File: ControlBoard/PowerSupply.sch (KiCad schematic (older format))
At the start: 6 parts, among them CON1 BARREL_JACK, J1 OrangePiPrime, M1 DC-DC_REG

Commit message: Revision 1.2 of the Control Board - All resisitors to 10k - Add solder jumpers to set i2c address - Move the GPIO +V line to 3.3V - Move pushbutton to PA6 as it has an interrupt associated with it - Update copyright year - Add OSHW & Inferno Embedded logos that was lost - Use SMD 28V zener for ESD protection on the 28V line - Use SMD 5.1V zener for ESD protection on the 5V line - Add a 2A polyswitch (fuse) to protect against overcurrent through the PSU - Switch the dc-dc footprint to SMD pads - Switch from electrolytic to ceramic caps (cheaper, easier to install) - Add a cutout for access to the serial header
Signed-off-by: Alastair D'Silva <alastair@d-silva.org>
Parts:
- added F1: Polyfuse, Fuse:Fuse_1206_3216Metric, symbol Device:Polyfuse
- C2: value 100uF -> 100uF 50V; footprint Capacitors_SMD:CP_Elec_6.3x7.7 -> Capacitor_SMD:C_1206_3216Metric
- C3, C4: value 100uF -> 100uF 16V; footprint Capacitors_SMD:CP_Elec_6.3x7.7 -> Capacitor_SMD:C_1206_3216Metric
- CON1: symbol conn:BARREL_JACK -> ControlBoard-rescue:BARREL_JACK-conn
- J1: symbol OrangePi:OrangePiPrime -> ControlBoard-rescue:OrangePiPrime-OrangePi
- M1: footprint D-Sun DC-DC Regulator:D-SUN_DC_DC -> DC-DC:D-SUN_DC_DC; symbol dc-dc_regulator:DC-DC_REG -> ControlBoard-rescue:DC-DC_REG-dc-dc_regulator
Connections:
- net +5V: now also F1.1; no longer M1.3 (OUT+)
- new net: F1.2, M1.3 (OUT+)
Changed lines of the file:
@@
 $EndDescr
 $Comp
-L conn:BARREL_JACK CON1
+L ControlBoard-rescue:BARREL_JACK-conn CON1
 U 1 1 5941132E
 P 1700 1150
@@
 	2100 1050 2100 950
 $Comp
-L OrangePi:OrangePiPrime J1
+L ControlBoard-rescue:OrangePiPrime-OrangePi J1
 U 1 1 5946954A
 P 1000 3400
+AR Path="/5946954A" Ref="J1"  Part="1"
+AR Path="/594691E7/5946954A" Ref="J1"  Part="1"
 F 0 "J1" H 1900 4500 60  0000 C CNN
 F 1 "OrangePiPrime" H 1350 4500 60  0000 C CNN
@@
 P 2400 1100
 F 0 "C2" H 2518 1146 50  0000 L CNN
-F 1 "100uF" H 2518 1055 50  0000 L CNN
-F 2 "Capacitors_SMD:CP_Elec_6.3x7.7" H 2438 950 50  0001 C CNN
+F 1 "100uF 50V" H 2518 1055 50  0000 L CNN
+F 2 "Capacitor_SMD:C_1206_3216Metric" H 2438 950 50  0001 C CNN
 F 3 "~" H 2400 1100 50  0001 C CNN
 	1    2400 1100
@@
 P 2550 3150
 F 0 "C3" H 2668 3196 50  0000 L CNN
-F 1 "100uF" H 2668 3105 50  0000 L CNN
-F 2 "Capacitors_SMD:CP_Elec_6.3x7.7" H 2588 3000 50  0001 C CNN
+F 1 "100uF 16V" H 2668 3105 50  0000 L CNN
+F 2 "Capacitor_SMD:C_1206_3216Metric" H 2588 3000 50  0001 C CNN
 F 3 "~" H 2550 3150 50  0001 C CNN
 	1    2550 3150
@@
 Connection ~ 1850 4250
 $Comp
-L dc-dc_regulator:DC-DC_REG M1
+L ControlBoard-rescue:DC-DC_REG-dc-dc_regulator M1
 U 1 1 5BE5E7C7
 P 4650 1450
 F 0 "M1" H 4650 2037 60  0000 C CNN
 F 1 "DC-DC_REG" H 4650 1931 60  0000 C CNN
-F 2 "D-Sun DC-DC Regulator:D-SUN_DC_DC" H 4650 1450 60  0001 C CNN
+F 2 "DC-DC:D-SUN_DC_DC" H 4650 1450 60  0001 C CNN
 F 3 "" H 4650 1450 60  0000 C CNN
 	1    4650 1450
@@
 P 3050 2650
 F 0 "C4" H 3168 2696 50  0000 L CNN
-F 1 "100uF" H 3168 2605 50  0000 L CNN
-F 2 "Capacitors_SMD:CP_Elec_6.3x7.7" H 3088 2500 50  0001 C CNN
+F 1 "100uF 16V" H 3168 2605 50  0000 L CNN
+F 2 "Capacitor_SMD:C_1206_3216Metric" H 3088 2500 50  0001 C CNN
 F 3 "~" H 3050 2650 50  0001 C CNN
 	1    3050 2650
@@
 L power:+5V #PWR0107
 U 1 1 5BE6087B
-P 5650 1100
-F 0 "#PWR0107" H 5650 950 50  0001 C CNN
-F 1 "+5V" H 5650 1240 50  0000 C CNN
-F 2 "" H 5650 1100 50  0000 C CNN
-F 3 "" H 5650 1100 50  0000 C CNN
-	1    5650 1100
-	1    0    0    -1
-$EndComp
-Wire Wire Line
-	5550 1250 5650 1250
-Wire Wire Line
-	5650 1250 5650 1100
+P 6200 1150
+F 0 "#PWR0107" H 6200 1000 50  0001 C CNN
+F 1 "+5V" H 6200 1290 50  0000 C CNN
+F 2 "" H 6200 1150 50  0000 C CNN
+F 3 "" H 6200 1150 50  0000 C CNN
+	1    6200 1150
+	1    0    0    -1
+$EndComp
+$Comp
+L Device:Polyfuse F1
+U 1 1 5C4B0AB6
+P 5900 1250
+F 0 "F1" V 5675 1250 50  0000 C CNN
+F 1 "Polyfuse" V 5766 1250 50  0000 C CNN
+F 2 "Fuse:Fuse_1206_3216Metric" H 5950 1050 50  0001 L CNN
+F 3 "~" H 5900 1250 50  0001 C CNN
+	1    5900 1250
+	0    1    1    0
+$EndComp
+Wire Wire Line
+	5550 1250 5750 1250
+Wire Wire Line
+	6050 1250 6200 1250
+Wire Wire Line
+	6200 1250 6200 1150
 $EndSCHEMATC

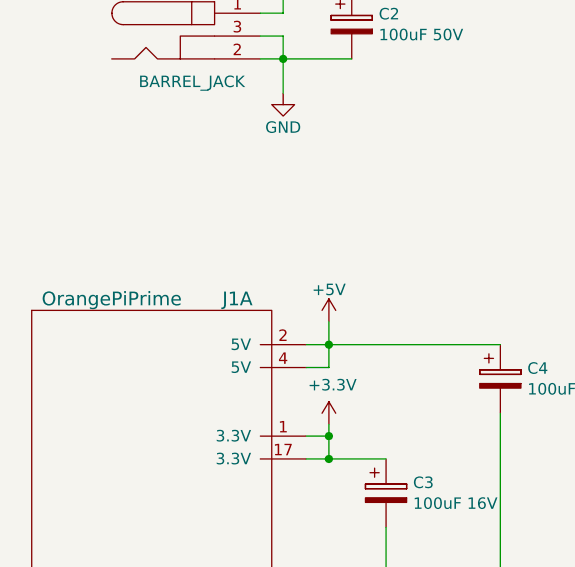
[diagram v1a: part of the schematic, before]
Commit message: Controlboard updates - Add second I2C port - Add Power LEDs (5V & 3.3V) - Add GPIO LED on PA2 - Add header for ST7735 LCD - Add missing mounting holes - Save OrangePiPrime footprints and symbols as explicit libs
Signed-off-by: Alastair D'Silva <alastair@d-silva.org>
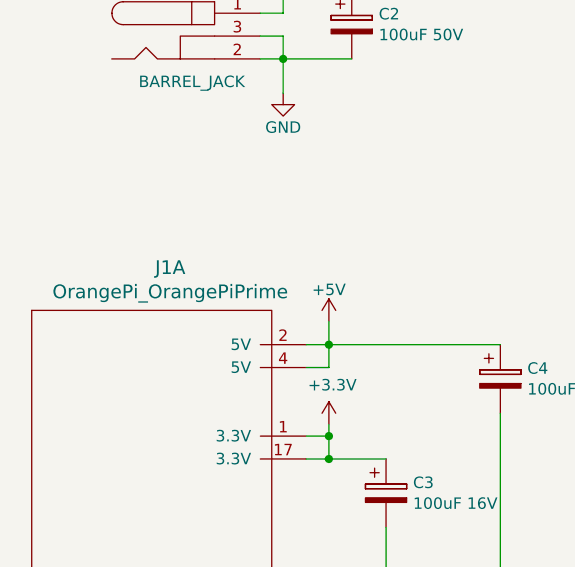
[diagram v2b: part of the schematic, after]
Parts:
- removed J1: OrangePiPrime, OrangePi:OrangePiPrime, symbol ControlBoard-rescue:OrangePiPrime-OrangePi
- added J1: OrangePi_OrangePiPrime, OrangePiPrime:OrangePiPrime, symbol OrangePiPrime:OrangePi_OrangePiPrime
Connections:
- net +3V3: now also J1.1 (3.3V), J1.17 (3.3V)
- net +5V: now also J1.2 (5V), J1.4 (5V)
- net GND: now also J1.14 (Gnd), J1.20 (Gnd), J1.25 (Gnd), J1.30 (Gnd), J1.34 (Gnd), J1.39 (Gnd), J1.6 (Gnd), J1.9 (Gnd)
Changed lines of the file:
@@
 	2100 1050 2100 950
-$Comp
-L ControlBoard-rescue:OrangePiPrime-OrangePi J1
-U 1 1 5946954A
-P 1000 3400
-AR Path="/5946954A" Ref="J1"  Part="1"
-AR Path="/594691E7/5946954A" Ref="J1"  Part="1"
-F 0 "J1" H 1900 4500 60  0000 C CNN
-F 1 "OrangePiPrime" H 1350 4500 60  0000 C CNN
-F 2 "OrangePi:OrangePiPrime" H 1000 3400 60  0001 C CNN
-F 3 "" H 1000 3400 60  0000 C CNN
-	1    1000 3400
-	1    0    0    -1
-$EndComp
 $Comp
 L power:+5V #PWR023
@@
 Wire Wire Line
 	6200 1250 6200 1150
+$Comp
+L OrangePiPrime:OrangePi_OrangePiPrime J1
+U 1 1 5C5C0884
+P 1000 3400
+F 0 "J1" H 1606 4637 60  0000 C CNN
+F 1 "OrangePi_OrangePiPrime" H 1606 4531 60  0000 C CNN
+F 2 "OrangePiPrime:OrangePiPrime" H 1000 3400 60  0001 C CNN
+F 3 "" H 1000 3400 60  0000 C CNN
+	1    1000 3400
+	1    0    0    -1
+$EndComp
 $EndSCHEMATC
